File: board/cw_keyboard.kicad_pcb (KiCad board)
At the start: 2 copper layers, 50 x 13 mm, 11 parts, among them J1 USB_A, U1 ATtiny44A-P, Y1 20MHz

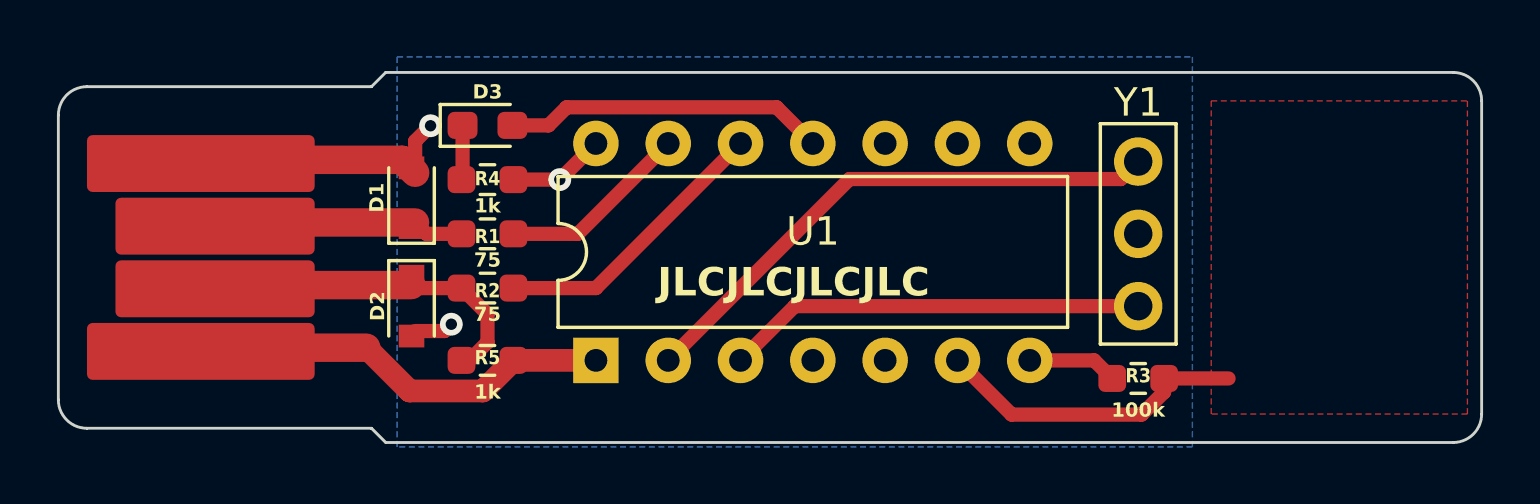
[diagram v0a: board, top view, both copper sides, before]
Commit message: feat: add bypass capacitor
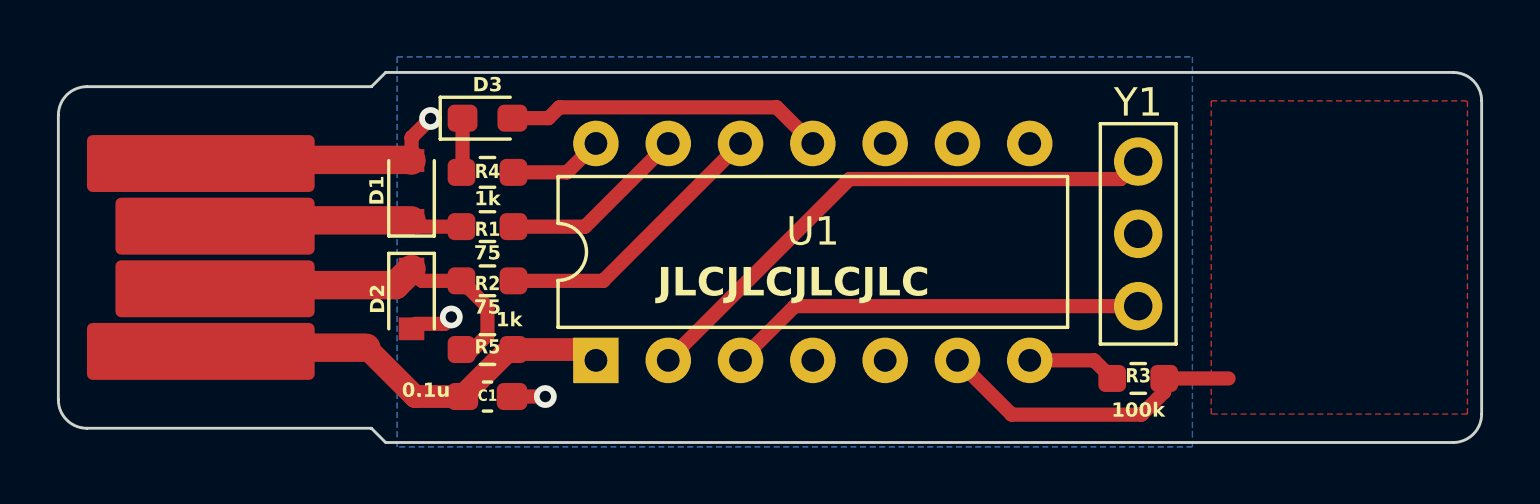
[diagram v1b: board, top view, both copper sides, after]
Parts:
- added C1: 0.1u, Capacitor_SMD:C_0603_1608Metric_Pad1.08x0.95mm_HandSolder, F.Cu at (28.6, 32.4)
- moved R5 0.38 mm to (28.6, 30.7)
- moved D2 0.25 mm to (25.9, 29.0)
- moved R1 0.25 mm to (28.6, 26.4)
- moved R4 0.25 mm to (28.6, 24.5)
- moved D1 0.25 mm to (25.9, 25.1)
- moved D3 0.25 mm to (28.6, 22.6)
- moved R2 0.25 mm to (28.6, 28.3)
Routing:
- net GND: track 14.4 -> 15.1 mm

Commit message: feat: add jumper to switch US/JIS layout
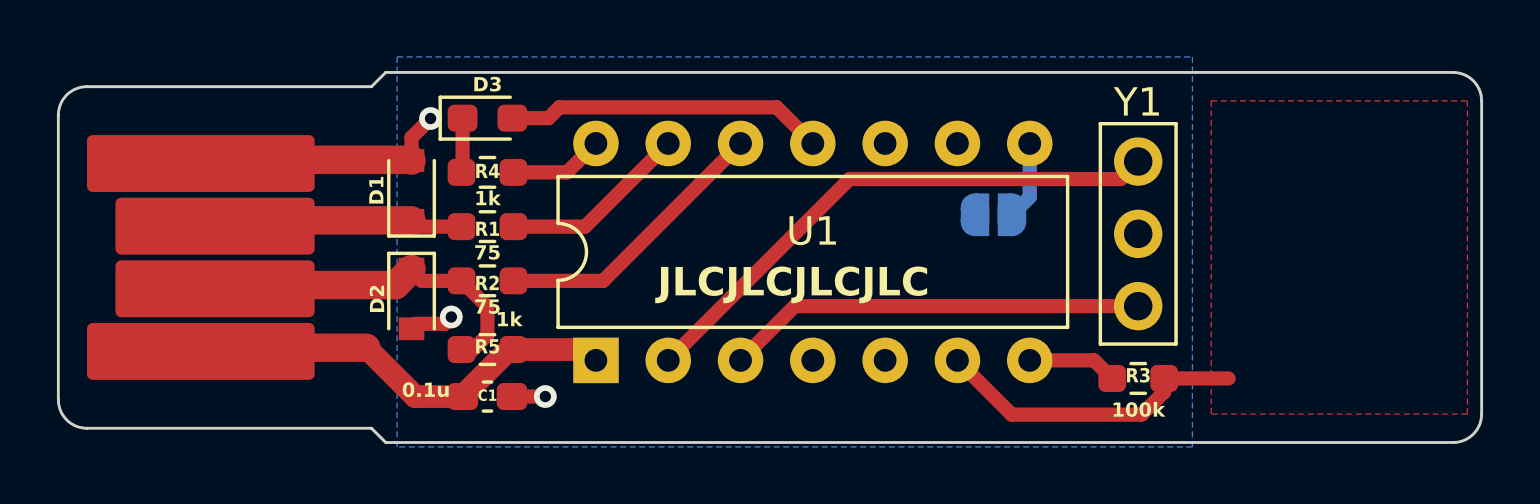
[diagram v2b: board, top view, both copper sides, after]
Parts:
- added JP1: SolderJumper_2_Open, Jumper:SolderJumper-2_P1.3mm_Open_RoundedPad1.0x1.5mm, B.Cu at (46.4, 26.0)
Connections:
- U1 pad 8: unconnected-(U1-PA5-Pad8) -> Net-(JP1-B)
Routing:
- net Net-(JP1-B): track 0.00 -> 2.76 mm
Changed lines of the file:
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@@
   (net 6 "TOUCHPAD")
   (net 7 "Net-(U1-PA6)")
-  (net 8 "unconnected-(U1-PA5-Pad8)")
+  (net 8 "Net-(JP1-B)")
   (net 9 "unconnected-(U1-PA4-Pad9)")
   (net 10 "unconnected-(U1-PA3-Pad10)")
@@
       (net 7 "Net-(U1-PA6)") (pinfunction "PA6") (pintype "bidirectional"))
     (pad "8" thru_hole oval (at 7.62 15.24 90) (size 1.6 1.6) (drill 0.8) (layers "*.Cu" "*.Mask")
-      (net 8 "unconnected-(U1-PA5-Pad8)") (pinfunction "PA5") (pintype "bidirectional"))
+      (net 8 "Net-(JP1-B)") (pinfunction "PA5") (pintype "bidirectional"))
     (pad "9" thru_hole oval (at 7.62 12.7 90) (size 1.6 1.6) (drill 0.8) (layers "*.Cu" "*.Mask")
       (net 9 "unconnected-(U1-PA4-Pad9)") (pinfunction "PA4") (pintype "bidirectional"))
@@
     )
   )
+  (footprint "Jumper:SolderJumper-2_P1.3mm_Open_RoundedPad1.0x1.5mm" (layer "B.Cu")
+    (at 46.35 26)
+    (descr "SMD Solder Jumper, 1x1.5mm, rounded Pads, 0.3mm gap, open")
+    (tags "solder jumper open")
+    (property "Sheetfile" "cw_keyboard.kicad_sch")
+    (property "Sheetname" "")
+    (property "ki_description" "Solder Jumper, 2-pole, open")
+    (property "ki_keywords" "solder jumper SPST")
+    (attr exclude_from_pos_files)
+    (fp_text reference "JP1" (at 0 1.8) (layer "Dwgs.User")
+        (effects (font (size 1 1) (thickness 0.15)) (justify mirror))
+    )
+    (fp_text value "SolderJumper_2_Open" (at 0 -1.9) (layer "B.Fab")
+        (effects (font (size 1 1) (thickness 0.15)) (justify mirror))
+    )
+    (fp_line (start -1.4 -0.3) (end -1.4 0.3)
+      (stroke (width 0.12) (type solid)) (layer "B.SilkS"))
+    (fp_line (start -0.7 1) (end 0.7 1)
+      (stroke (width 0.12) (type solid)) (layer "B.SilkS"))
+    (fp_line (start 0.7 -1) (end -0.7 -1)
+      (stroke (width 0.12) (type solid)) (layer "B.SilkS"))
+    (fp_line (start 1.4 0.3) (end 1.4 -0.3)
+      (stroke (width 0.12) (type solid)) (layer "B.SilkS"))
+    (fp_arc (start -1.4 -0.3) (mid -1.194975 -0.794975) (end -0.7 -1)
+      (stroke (width 0.12) (type solid)) (layer "B.SilkS"))
+    (fp_arc (start -0.7 1) (mid -1.194975 0.794975) (end -1.4 0.3)
+      (stroke (width 0.12) (type solid)) (layer "B.SilkS"))
+    (fp_arc (start 0.7 -1) (mid 1.194975 -0.794975) (end 1.4 -0.3)
+      (stroke (width 0.12) (type solid)) (layer "B.SilkS"))
+    (fp_arc (start 1.4 0.3) (mid 1.194975 0.794975) (end 0.7 1)
+      (stroke (width 0.12) (type solid)) (layer "B.SilkS"))
+    (fp_line (start -1.65 1.25) (end -1.65 -1.25)
+      (stroke (width 0.05) (type solid)) (layer "B.CrtYd"))
+    (fp_line (start -1.65 1.25) (end 1.65 1.25)
+      (stroke (width 0.05) (type solid)) (layer "B.CrtYd"))
+    (fp_line (start 1.65 -1.25) (end -1.65 -1.25)
+      (stroke (width 0.05) (type solid)) (layer "B.CrtYd"))
+    (fp_line (start 1.65 -1.25) (end 1.65 1.25)
+      (stroke (width 0.05) (type solid)) (layer "B.CrtYd"))
+    (pad "1" smd custom (at -0.65 0) (size 1 0.5) (layers "B.Cu" "B.Mask")
+      (net 14 "GND") (pinfunction "A") (pintype "passive") (zone_connect 2)
+      (options (clearance outline) (anchor rect))
+      (primitives
+        (gr_circle (center 0 -0.25) (end 0.5 -0.25) (width 0) (fill yes))
+        (gr_circle (center 0 0.25) (end 0.5 0.25) (width 0) (fill yes))
+        (gr_poly
+          (pts
+            (xy 0.5 -0.75)
+            (xy 0 -0.75)
+            (xy 0 0.75)
+            (xy 0.5 0.75)
+          )
+          (width 0) (fill yes))
+      ))
+    (pad "2" smd custom (at 0.65 0) (size 1 0.5) (layers "B.Cu" "B.Mask")
+      (net 8 "Net-(JP1-B)") (pinfunction "B") (pintype "passive") (zone_connect 2)
+      (options (clearance outline) (anchor rect))
+      (primitives
+        (gr_circle (center 0 -0.25) (end 0.5 -0.25) (width 0) (fill yes))
+        (gr_circle (center 0 0.25) (end 0.5 0.25) (width 0) (fill yes))
+        (gr_poly
+          (pts
+            (xy 0 -0.75)
+            (xy -0.5 -0.75)
+            (xy -0.5 0.75)
+            (xy 0 0.75)
+          )
+          (width 0) (fill yes))
+      ))
+  )
   (gr_poly
     (pts
@@
   (segment (start 47.625 31.115) (end 49.8875 31.115) (width 0.5) (layer "F.Cu") (net 7))
   (segment (start 49.8875 31.115) (end 50.5225 31.75) (width 0.5) (layer "F.Cu") (net 7))
+  (segment (start 47.625 25.375) (end 47 26) (width 0.5) (layer "B.Cu") (net 8))
+  (segment (start 47.625 23.495) (end 47.625 25.375) (width 0.5) (layer "B.Cu") (net 8))
   (segment (start 29.45 22.606) (end 30.72 22.606) (width 0.5) (layer "F.Cu") (net 11))
   (segment (start 31.101 22.225) (end 38.735 22.225) (width 0.5) (layer "F.Cu") (net 11))

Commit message: fix: twist pair distance
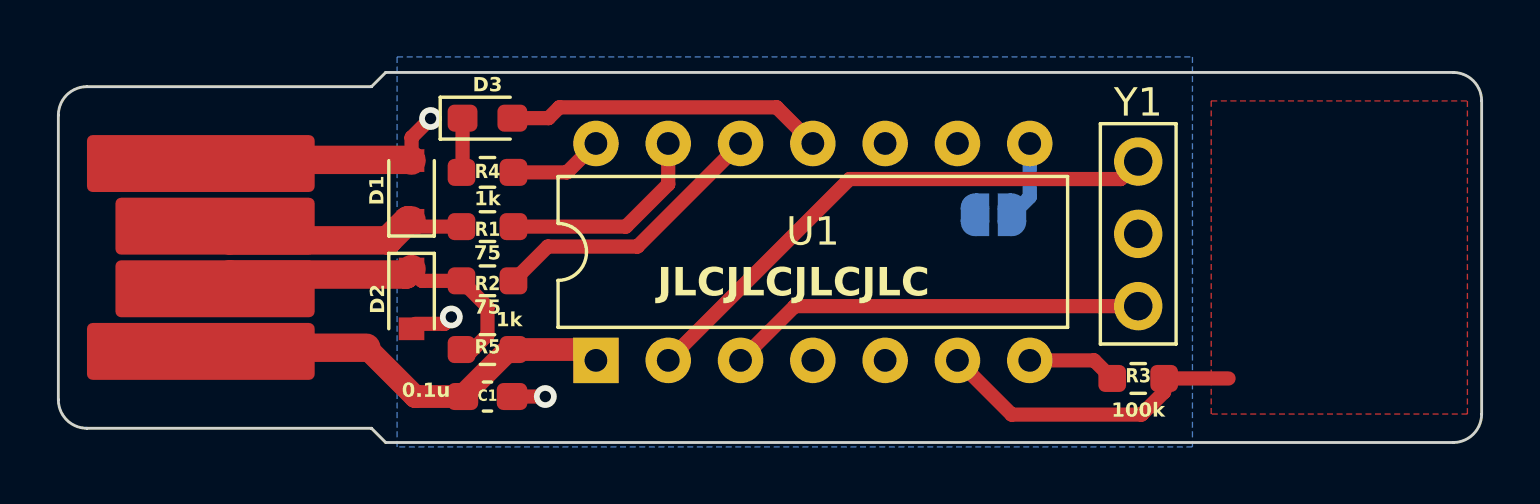
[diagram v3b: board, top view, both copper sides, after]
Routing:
- net Net-(U1-AREF/PA0): track 6.65 -> 7.49 mm
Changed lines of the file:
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@@
   (segment (start 38.735 22.225) (end 40.005 23.495) (width 0.5) (layer "F.Cu") (net 11))
   (segment (start 30.72 22.606) (end 31.101 22.225) (width 0.5) (layer "F.Cu") (net 11))
-  (segment (start 29.4875 28.321) (end 32.639 28.321) (width 0.5) (layer "F.Cu") (net 12))
-  (segment (start 32.639 28.321) (end 37.465 23.495) (width 0.5) (layer "F.Cu") (net 12))
-  (segment (start 32.004 26.416) (end 29.4875 26.416) (width 0.5) (layer "F.Cu") (net 13))
-  (segment (start 34.925 23.495) (end 32.004 26.416) (width 0.5) (layer "F.Cu") (net 13))
+  (segment (start 29.4875 28.321) (end 30.6925 27.116) (width 0.5) (layer "F.Cu") (net 12))
+  (segment (start 33.844 27.116) (end 37.465 23.495) (width 0.5) (layer "F.Cu") (net 12))
+  (segment (start 30.6925 27.116) (end 33.844 27.116) (width 0.5) (layer "F.Cu") (net 12))
+  (segment (start 33.439 26.416) (end 29.4875 26.416) (width 0.5) (layer "F.Cu") (net 13))
+  (segment (start 34.925 23.495) (end 34.925 24.93) (width 0.5) (layer "F.Cu") (net 13))
+  (segment (start 34.925 24.93) (end 33.439 26.416) (width 0.5) (layer "F.Cu") (net 13))
   (segment (start 18.505 24.2) (end 18.635 24.07) (width 1) (layer "F.Cu") (net 14))
   (segment (start 25.908 23.285825) (end 26.5755 22.618325) (width 0.5) (layer "F.Cu") (net 14))
@@
   (via (at 30.607 32.385) (size 0.8) (drill 0.4) (layers "F.Cu" "B.Cu") (free) (net 14))
   (via (at 26.5755 22.618325) (size 0.8) (drill 0.4) (layers "F.Cu" "B.Cu") (free) (net 14))
+  (segment (start 25.77805 26.196) (end 25.07405 26.9) (width 1) (layer "F.Cu") (net 15))
   (segment (start 27.6625 26.416) (end 26.128 26.416) (width 0.5) (layer "F.Cu") (net 15))
+  (segment (start 25.07405 26.9) (end 19.505 26.9) (width 1) (layer "F.Cu") (net 15))
   (segment (start 26.128 26.416) (end 25.908 26.196) (width 0.5) (layer "F.Cu") (net 15))
-  (segment (start 25.908 26.196) (end 19.209 26.196) (width 1) (layer "F.Cu") (net 15))
-  (segment (start 19.209 26.196) (end 19.005 26.4) (width 1) (layer "F.Cu") (net 15))
+  (segment (start 25.908 26.196) (end 25.77805 26.196) (width 1) (layer "F.Cu") (net 15))
+  (segment (start 19.505 26.9) (end 19.005 26.4) (width 1) (layer "F.Cu") (net 15))
+  (segment (start 19.505 28.1) (end 25.714 28.1) (width 1) (layer "F.Cu") (net 16))
   (segment (start 27.6625 28.321) (end 28.575 29.2335) (width 0.5) (layer "F.Cu") (net 16))
   (segment (start 28.575 30.226) (end 27.94 30.861) (width 0.5) (layer "F.Cu") (net 16))
   (segment (start 25.9 28.216) (end 26.035 28.081) (width 0.5) (layer "F.Cu") (net 16))
-  (segment (start 19.005 28.6) (end 19.135 28.47) (width 1) (layer "F.Cu") (net 16))
+  (segment (start 19.005 28.6) (end 19.505 28.1) (width 1) (layer "F.Cu") (net 16))
   (segment (start 27.6625 28.321) (end 26.275 28.321) (width 0.5) (layer "F.Cu") (net 16))
-  (segment (start 19.135 28.47) (end 25.344 28.47) (width 1) (layer "F.Cu") (net 16))
-  (segment (start 25.344 28.47) (end 25.908 27.906) (width 1) (layer "F.Cu") (net 16))
+  (segment (start 25.714 28.1) (end 25.908 27.906) (width 1) (layer "F.Cu") (net 16))
   (segment (start 27.94 30.861) (end 27.6625 30.861) (width 0.5) (layer "F.Cu") (net 16))
   (segment (start 26.275 28.321) (end 26.035 28.081) (width 0.5) (layer "F.Cu") (net 16))
